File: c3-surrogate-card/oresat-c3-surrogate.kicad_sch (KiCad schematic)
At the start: 74 parts, among them J1 J-SAMTEC-TFM-120-X1-XXX-D-RA, J2 Conn_01x04, J3 1900468, J4 1995499, Q1 PMV45EN, Q3 NTR4101P, Q4 NTR4101P, Q5 DMP3050LVT-7, SW2 EG1218, SW3 OS203011MV9QS1, SW4 EG1218, U1 MAX892LEUA+T, U2 LTC4412xS6, U4 LTC4412xS6, U5 TS5A21366

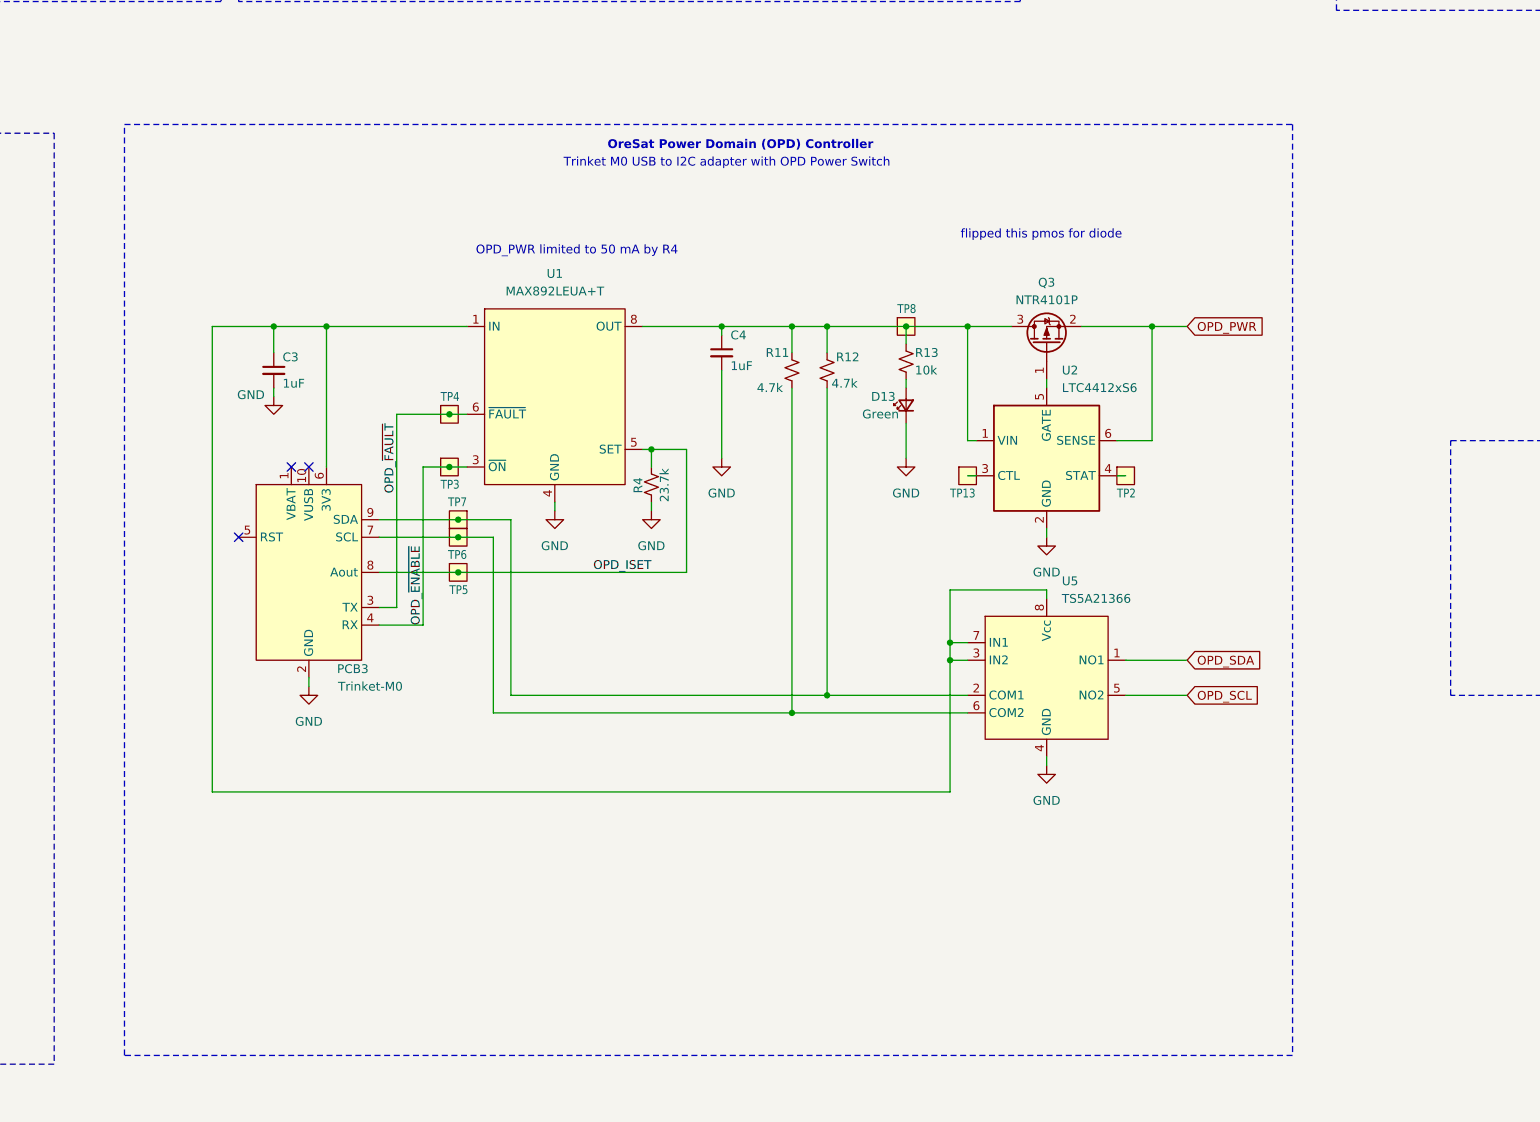
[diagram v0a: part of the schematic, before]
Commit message: Updated Trinket M0 symbol to be sane and update with pinout picture.
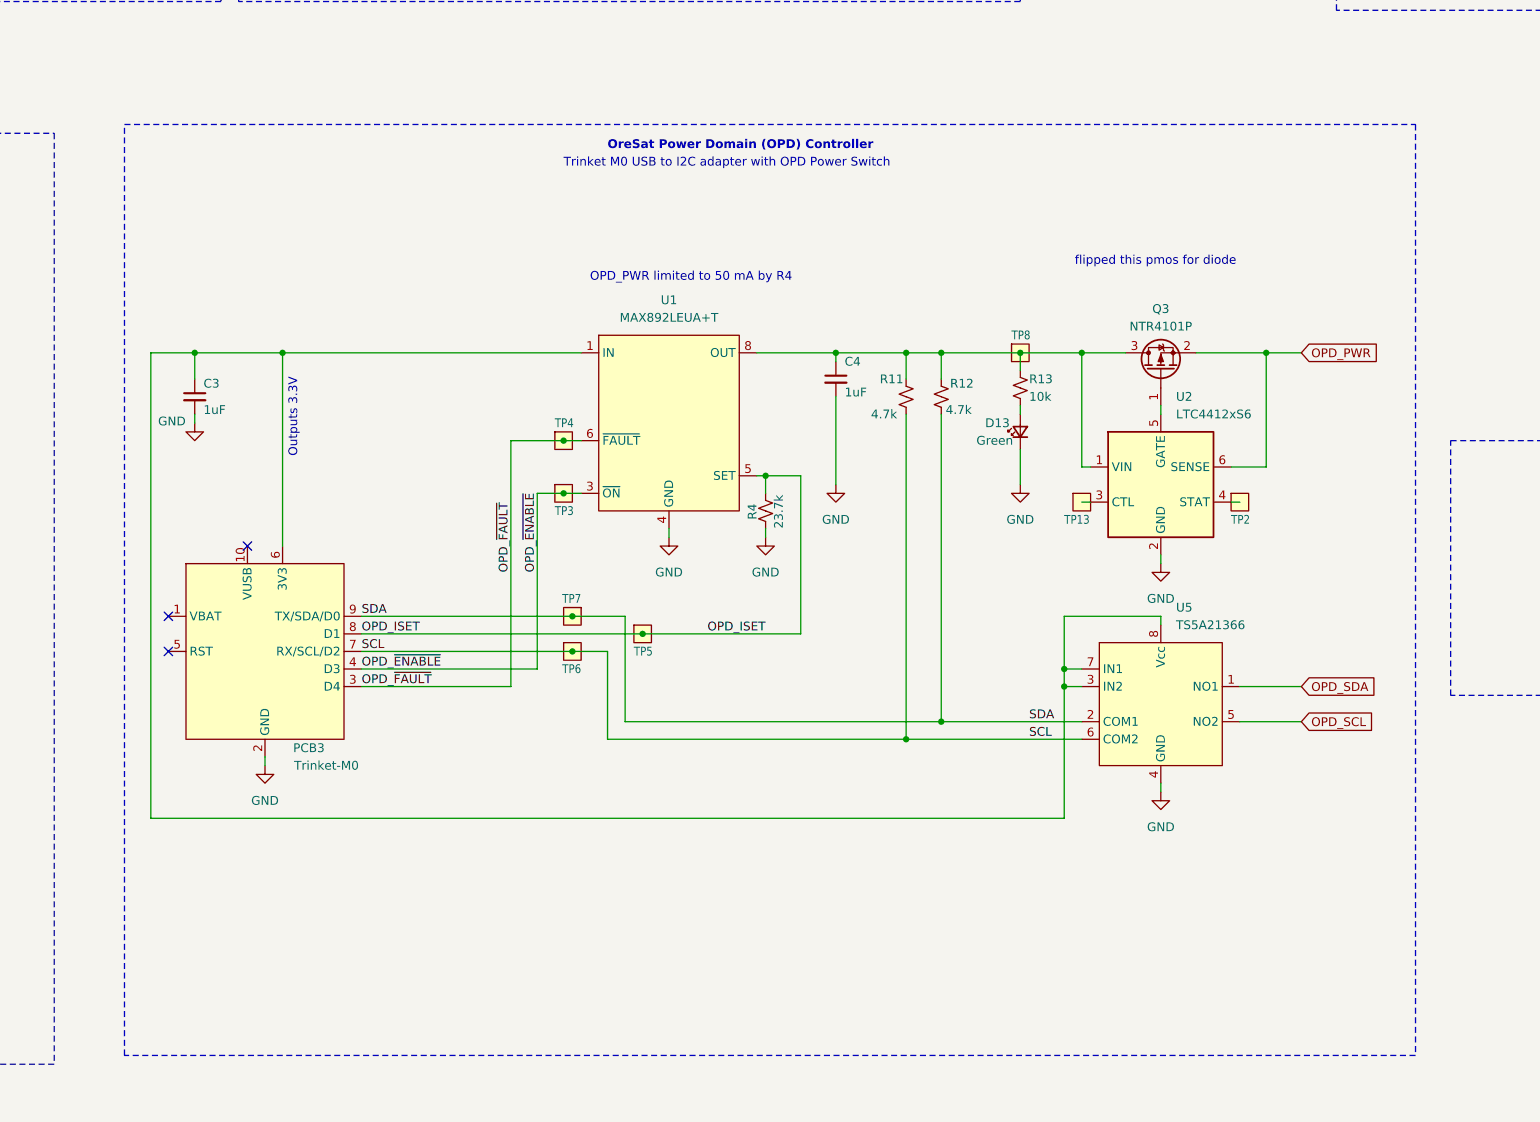
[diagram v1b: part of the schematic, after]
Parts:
- PCB3: footprint oresat-pcbs:Adafruit-Trinket -> Adafruit-Trinket-M0:Trinket-M0
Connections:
- net SCL: now reaches PCB3.7 (RX/SCL/D2), R11.2, TP6.1, U5.6 (COM2)
- net SDA: now reaches PCB3.9 (TX/SDA/D0), R12.2, TP7.1, U5.2 (COM1)
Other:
- note added: "Outputs 3.3V"
- moved on the sheet: C3, C4, D13, PCB3, Q3, R11, R12, R13, R4, TP13, TP2, TP3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
